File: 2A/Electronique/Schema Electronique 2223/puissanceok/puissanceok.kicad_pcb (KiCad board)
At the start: 4 copper layers, 66 x 57 mm, 66 parts, among them J10 Conn_01x05, J11 Conn_01x02, J12 Conn_01x02, J13 Conn_01x02, J14 Conn_01x02, J15 Conn_01x02, J16 Conn_01x02, J17 Conn_01x02, J18 Conn_01x02, J19 Conn_01x02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

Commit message: finalize schematic + footprints
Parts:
- added C1: 10u, Capacitor_SMD:CP_Elec_4x5.4, F.Cu at (192.4, 52.0)
- added C10: 47u, Capacitor_SMD:CP_Elec_6.3x5.4, F.Cu at (158.3, 32.4)
- added C15: 100u, Capacitor_SMD:CP_Elec_6.3x7.7, F.Cu at (181.3, 47.6)
- added C3: 100u, Capacitor_SMD:CP_Elec_6.3x7.7, F.Cu at (191.9, 32.4)
- added C4: 47u, Capacitor_SMD:CP_Elec_6.3x5.4, F.Cu at (181.4, 32.4)
- added C9: 100u, Capacitor_SMD:CP_Elec_6.3x7.7, F.Cu at (168.8, 32.4)
- added D1: TVS 20.5V, Diode_SMD:D_SMB, F.Cu at (192.7, 46.3)
- added D302: D_Schottky, custom:DST10100S, F.Cu at (192.1, 39.0)
- added D602: D_Schottky, custom:DST10100S, F.Cu at (169.0, 39.0)
- added J1: AU, custom:691322110002, F.Cu at (62.1, 94.6)
- added J3: Bat 2, custom:691322110002, F.Cu at (81.0, 94.6)
- added J4: Bat 1, custom:691322110002, F.Cu at (90.5, 94.6)
- added U1: LT1076CR-PBF, Package_TO_SOT_SMD:TO-263-7_TabPin4, F.Cu at (186.8, 22.1)
- added U2: LT1076CR-PBF, Package_TO_SOT_SMD:TO-263-7_TabPin4, F.Cu at (163.7, 22.1)
- added U3: 74LVC2G241, Package_SO:VSSOP-8_2.3x2mm_P0.5mm, F.Cu at (178.8, 53.5)
- H1, H2, H3, H4: footprint MountingHole:MountingHole_3.2mm_M3_Pad_Via -> MountingHole:MountingHole_2.7mm_M2.5_Pad_Via
- J11: value Conn_01x02 -> Conn_Phidget_PS_Stepper_1
- J13: value Conn_01x02 -> Conn_Phidget_PS_Stepper_2
- J14: value Conn_01x02 -> Conn_Phidget_PS_Stepper_3
- J15: value Conn_01x02 -> Conn_Phidget_PS_Stepper_4
- J16, J17, J18, J19: value Conn_01x02 -> Conn_FDC
- J2: value Raspberry PI -> Switch; footprint Connector_PinSocket_2.54mm:PinSocket_2x20_P2.54mm_Vertical -> custom:691322110002; moved to F.Cu
- J20, J22, J23: value Conn_01x04 -> Conn_UART
- J21: value Conn_01x03 -> Conn_XL320
- J5: value Conn_01x08 -> Conn_GND
- J6: value Conn_01x08 -> Conn_GPIO_unused
- J7: value Conn_01x08 -> Conn_3.3V
- J8: value Conn_02x20_Odd_Even -> Conn_RPI; moved to B.Cu
- L1, L2: value 22uH -> 22m; footprint Inductor_SMD:L_0805_2012Metric_Pad1.05x1.20mm_HandSolder -> Inductor_SMD:L_Changjiang_FNR8065S
- R1, R10, R11, R12, R13, R14, R15, R16, R17, R18, R19, R2, R20, R21, R3, R4, R5, R6, R7, R8, R9: footprint Resistor_SMD:R_0603_1608Metric_Pad0.98x0.95mm_HandSolder -> Resistor_SMD:R_0402_1005Metric
- moved J8 203.8 mm to (54.9, 51.3)
- moved ? 57.7 mm to (50.0, 99.0)
- moved H1 57.7 mm to (50.0, 50.0)
- moved H4 57.7 mm to (50.0, 99.0)
- moved H2 57.7 mm to (108.0, 50.0)
- moved H3 57.7 mm to (108.0, 99.0)
- moved L1 52.3 mm to (179.5, 70.6)
- moved L2 52.3 mm to (189.0, 70.6)
- moved J2 46.8 mm to (71.5, 94.6), turned to 0 degrees
- moved J5 21.3 mm to (240.9, 54.9)
- moved J6 21.3 mm to (240.9, 57.5)
- moved J7 21.3 mm to (240.9, 60.0)
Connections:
- J10 pad 1: /out_color_sensor -> /Out_color_sensor
- J2 pad 1: (no net) -> Net-(J1-Pin_2)
- J2 pad 2: (no net) -> Vin

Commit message: version 1 placement composants
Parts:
- moved J11 206.9 mm to (50.3, 64.0)
- moved J20 201.3 mm to (56.2, 88.9), turned to 0 degrees
- moved J13 191.3 mm to (50.3, 72.5)
- moved J14 183.8 mm to (50.3, 81.2)
- moved J15 176.8 mm to (50.3, 89.8)
- moved J12 153.8 mm to (98.3, 98.7), turned to 0 degrees
- moved J21 151.1 mm to (96.7, 88.9), turned to 0 degrees
- moved J19 142.9 mm to (107.7, 83.9), turned to 90 degrees
- moved C1 135.2 mm to (69.2, 107.8)
- moved J22 133.0 mm to (69.7, 88.9), turned to 0 degrees
- moved J16 127.6 mm to (107.7, 75.3), turned to 90 degrees
- moved J18 122.6 mm to (107.7, 92.5), turned to 90 degrees
- moved J23 121.9 mm to (83.2, 88.9), turned to 0 degrees
- moved J5 119.1 mm to (124.4, 30.2)
- moved J6 119.1 mm to (124.4, 32.7)
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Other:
- board text added: "3.3v"
- board text added: "U2"
- board text added: "buffer"
- board text added: "capteur couleur"
- board text added: "u1"

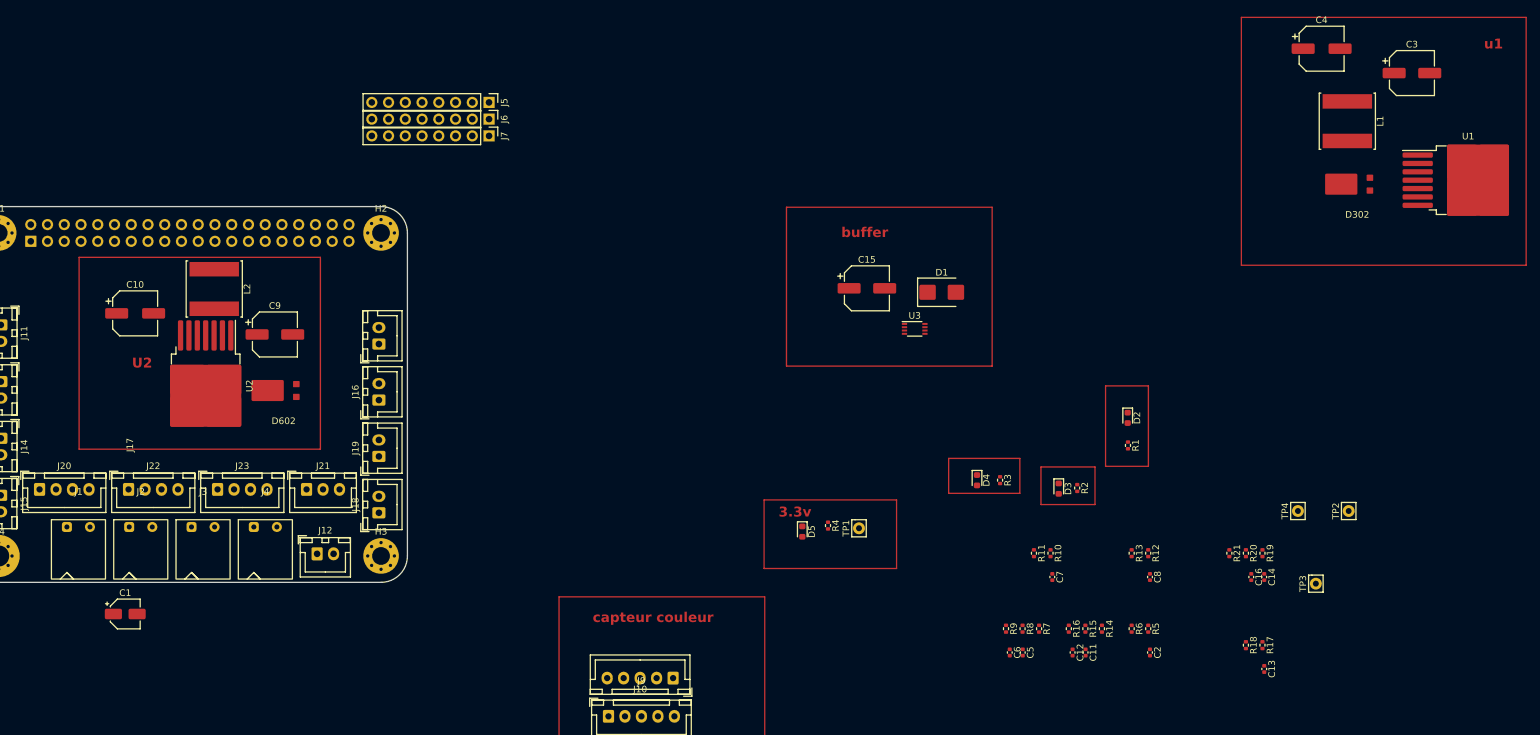
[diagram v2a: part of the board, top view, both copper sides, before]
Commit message: trie des composants, placement des composants
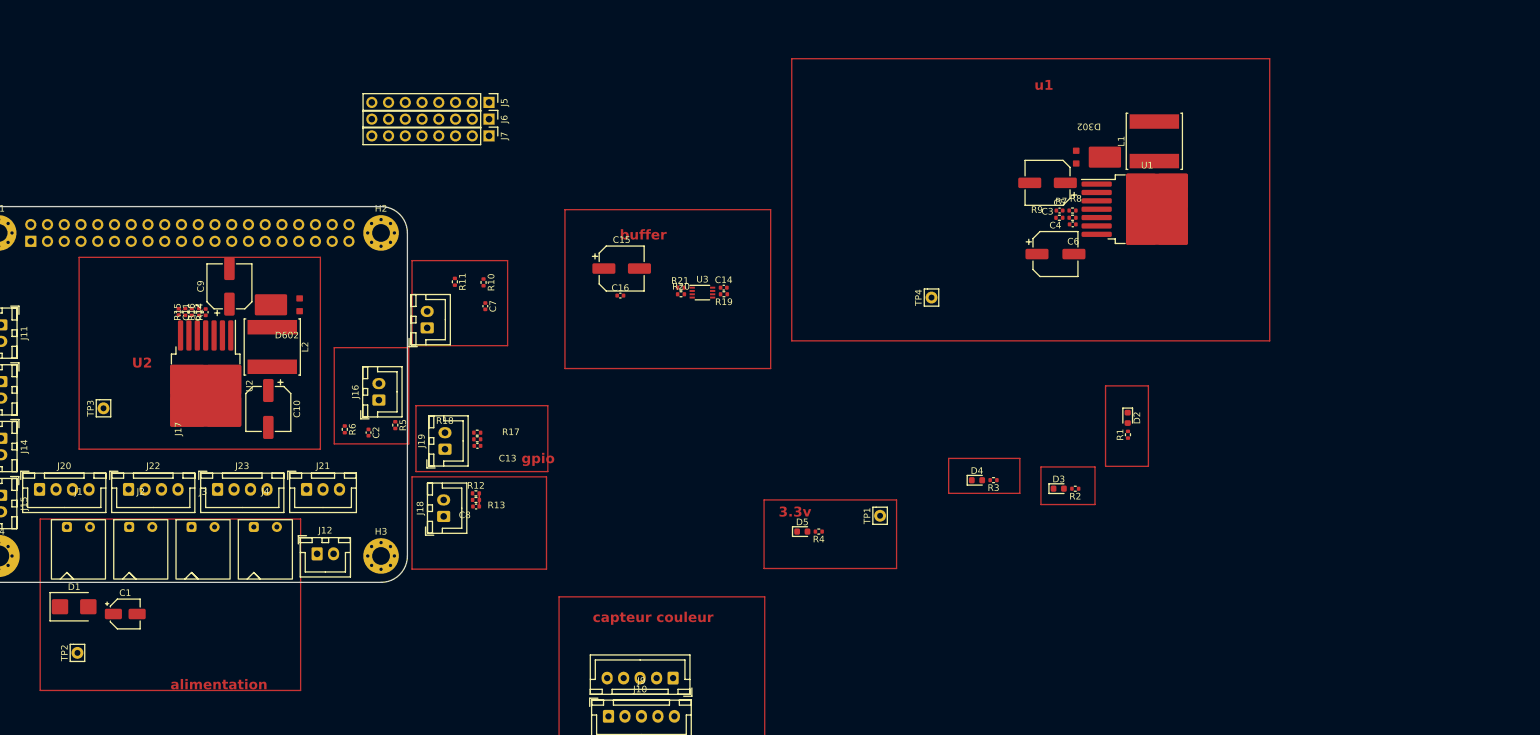
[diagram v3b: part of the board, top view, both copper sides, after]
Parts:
- R7: value 2k87 -> 3k52
- R9: value 2k2 -> 1k5
- moved TP2 194.0 mm to (62.0, 113.7)
- moved TP3 185.8 mm to (65.9, 76.6)
- moved C11 146.9 mm to (77.3, 62.0)
- moved R14 146.2 mm to (79.3, 62.0)
- moved R15 144.7 mm to (78.3, 62.0), turned to 90 degrees
- moved C12 141.3 mm to (81.4, 62.0), turned to 90 degrees
- moved R16 140.4 mm to (80.4, 62.0), turned to 90 degrees
- moved D1 140.0 mm to (61.5, 106.7)
- moved C13 124.1 mm to (122.6, 82.3), turned to 180 degrees
- moved C2 123.1 mm to (106.1, 80.3)
- moved R17 123.1 mm to (122.6, 81.3), turned to 0 degrees
- moved R6 123.1 mm to (102.5, 79.8)
- moved R18 121.0 mm to (122.6, 80.3), turned to 0 degrees
- moved R5 118.3 mm to (110.2, 79.2)
- moved C16 104.8 mm to (144.3, 59.5), turned to 0 degrees
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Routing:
- net /FDC_1: track 0.00 -> 2.01 mm
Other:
- board text added: "alimentation"
- board text added: "gpio"

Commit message: update pcb and schematic
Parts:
- C1, C13, C16, C2, C7, C8, D1, R10, R11, R12, R13, R17, R18, R5, R6: moved to B.Cu
- moved U1 161.8 mm to (63.2, 62.4), turned to 180 degrees
- moved L1 146.1 mm to (82.0, 64.7), turned to 0 degrees
- moved D302 142.4 mm to (75.5, 65.8), turned to -90 degrees
- moved R9 139.5 mm to (73.9, 59.2), turned to -90 degrees
- moved R8 138.9 mm to (74.4, 56.8), turned to 0 degrees
- moved C6 138.4 mm to (74.9, 59.2), turned to -90 degrees
- moved R7 136.9 mm to (74.4, 57.8), turned to 180 degrees
- moved C5 135.5 mm to (75.8, 56.3), turned to 90 degrees
- moved C3 128.6 mm to (81.3, 56.7), turned to 0 degrees
- moved C4 120.4 mm to (90.1, 60.6), turned to 90 degrees
- moved J10 102.1 mm to (60.9, 72.1), turned to 0 degrees
- moved J9 83.7 mm to (70.8, 80.0), turned to 180 degrees
- moved C14 81.4 mm to (81.3, 79.0), turned to 180 degrees
- moved R19 80.1 mm to (82.8, 80.5), turned to -90 degrees
- moved R20 79.8 mm to (76.7, 81.0)
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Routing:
- net /FDC_1: track 2.01 -> 0.00 mm
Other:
- board text added: "11"
- board text added: "16"
- board text added: "19"
- board text added: "2"
- board text added: "20"
- board text added: "21"
- board text added: "3"
- board text added: "6"
- board text added: "Conn_Phidget_PS_Stepper"
- board text removed: "buffer"
- board text removed: "capteur couleur"

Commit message: update pcb
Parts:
- C10, C11, C12, C9, D602, R14, R15, R16, U2: moved to B.Cu
- R7: value 3k52 -> 2k87
- R9: value 1k5 -> 2k2
- moved D2 127.1 mm to (103.3, 77.5), turned to 0 degrees
- moved R1 124.7 mm to (106.2, 77.5), turned to 180 degrees
- moved D3 119.8 mm to (103.3, 73.5)
- moved R2 119.3 mm to (106.3, 73.7)
- moved D4 108.6 mm to (103.3, 70.0)
- moved R3 108.2 mm to (106.3, 70.0)
- moved TP1 93.5 mm to (108.7, 66.5)
- moved D5 88.9 mm to (103.4, 66.5)
- moved R4 88.6 mm to (106.3, 66.6)
- moved J12 62.2 mm to (97.5, 73.5), turned to -90 degrees
- moved TP3 58.0 mm to (108.7, 70.0)
- moved C11 49.6 mm to (89.5, 69.5)
- moved R15 47.4 mm to (89.5, 67.5), turned to -90 degrees
- moved R14 46.5 mm to (91.2, 66.2), turned to 90 degrees
- moved D602 45.2 mm to (95.5, 62.8)
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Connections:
- D302 pad ²: Net-(D302-K) -> (no net)
- J9 pad 1: 3V3 -> +3.3V
- J9 pad 4: 5V -> 5.1V
- R1 pad 1: 14.4V -> Vin
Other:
- board text removed: "3.3v"
- board text removed: "U2"
- board text removed: "u1"

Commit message: version2 placements composants
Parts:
- C1, C10, C11, C12, C13, C16, C2, C7, C8, C9, D1, D602, R10, R11, R12, R13, R14, R15, R16, R17, R18, R5, R6, U2: moved to F.Cu
- moved J12 51.8 mm to (49.3, 92.7), turned to 90 degrees
- moved J10 48.9 mm to (101.2, 99.7), turned to 180 degrees
- moved J21 36.5 mm to (56.8, 90.9), turned to 0 degrees
- moved C5 24.5 mm to (69.9, 80.0)
- moved R8 23.9 mm to (68.9, 80.1), turned to -90 degrees
- moved J9 23.5 mm to (91.2, 91.8), turned to 0 degrees
- moved J20 23.5 mm to (94.9, 78.4), turned to -90 degrees
- moved R7 23.2 mm to (67.9, 80.1), turned to 90 degrees
- moved J18 23.1 mm to (101.7, 61.2)
- moved J22 23.0 mm to (101.7, 78.4), turned to -90 degrees
- moved C16 22.7 mm to (65.8, 83.6)
- moved R17 21.9 mm to (97.0, 68.2), turned to 90 degrees
- moved C15 21.4 mm to (60.5, 83.6)
- moved C6 21.2 mm to (70.9, 80.0), turned to 90 degrees
- moved R9 20.9 mm to (71.9, 80.0), turned to 90 degrees
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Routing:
- added copper zone on In2.Cu, net GND

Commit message: update
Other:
- board text removed: "alimentation"
- board text removed: "gpio"
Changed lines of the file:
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@@
   (gr_line locked (start 50 103) (end 108 103)
     (stroke (width 0.1) (type default)) (layer "Edge.Cuts"))
-  (gr_text "gpio" (at 114 86.05 90) (layer "F.Cu")
-    (effects (font (size 1.5 1.5) (thickness 0.3) bold) (justify left bottom))
-  )
-  (gr_text "alimentation" (at 42.25 70.25 -90) (layer "F.Cu")
-    (effects (font (size 1.5 1.5) (thickness 0.3) bold) (justify left bottom))
-  )
   (gr_text "Conn_Phidget_PS_Stepper" (at 61.555 95.2) (layer "F.SilkS")
     (effects (font (size 0.8 0.8) (thickness 0.125)) (justify left bottom))
